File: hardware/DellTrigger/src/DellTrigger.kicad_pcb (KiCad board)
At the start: 2 copper layers, 30 x 12 mm, 11 parts, among them U1 U Eeprom DS2502 (TO92H)

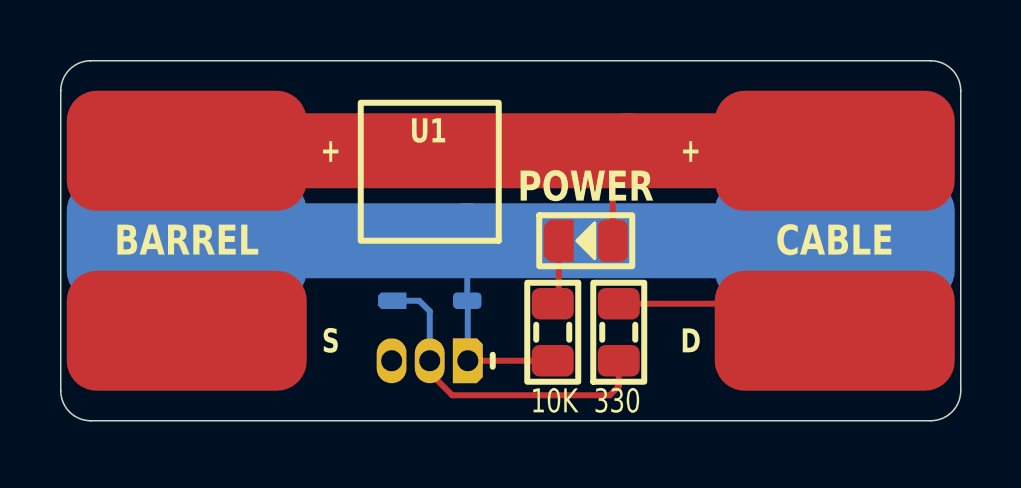
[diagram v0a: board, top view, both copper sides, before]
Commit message: Added DellTrigger schematics
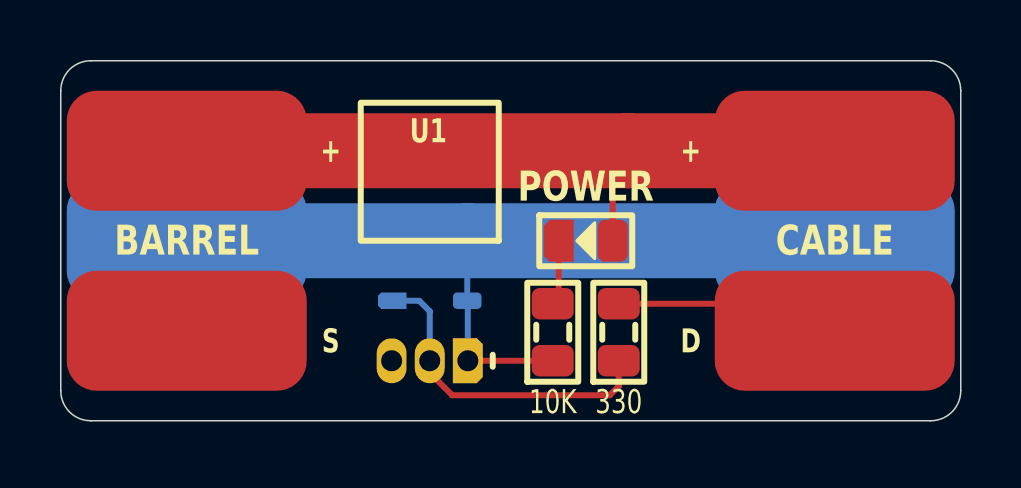
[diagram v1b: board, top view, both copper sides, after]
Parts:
- turned R2 to 90 degrees
- gave numbers to parts that had none: 6
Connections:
- net 20V renamed +VDC
- R2 pad 1: LED -> GND
- R2 pad 2: GND -> LED
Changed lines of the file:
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@@
 	(net 0 "")
 	(net 1 "GND")
-	(net 2 "20V")
+	(net 2 "DATA'")
 	(net 3 "DATA")
-	(net 4 "DATA'")
-	(net 5 "LED")
+	(net 4 "LED")
+	(net 5 "+VDC")
 	(footprint "Medo64:TP Pad (8.0x4.0)"
 		(locked yes)
@@
 		(at 40.8 18)
 		(descr "Keystone 5016")
-		(property "Reference" "TP?"
+		(property "Reference" "TP21"
 			(at 0 -3 0)
 			(layer "F.SilkS")
@@
 			(layers "F.Cu" "F.Mask")
 			(roundrect_rratio 0.25)
-			(net 2 "20V")
+			(net 5 "+VDC")
 		)
 	)
@@
 		(at 19.2 18)
 		(descr "Keystone 5016")
-		(property "Reference" "TP?"
+		(property "Reference" "TP11"
 			(at 0 -3 0)
 			(layer "F.SilkS")
@@
 			(layers "F.Cu" "F.Mask")
 			(roundrect_rratio 0.25)
-			(net 2 "20V")
+			(net 5 "+VDC")
 		)
 	)
@@
 			)
 		)
+		(property ki_fp_filters "LED* LED_SMD:* LED_THT:*")
+		(sheetname "Root")
+		(sheetfile "DellTrigger.kicad_sch")
 		(attr smd)
 		(fp_rect
@@
 			(chamfer_ratio 0.2)
 			(chamfer top_left bottom_left)
-			(net 5 "LED")
+			(net 4 "LED")
+			(pinfunction "K")
+			(pintype "passive")
 			(thermal_bridge_angle 45)
 		)
@@
 			(layers "F.Cu" "F.Paste" "F.Mask")
 			(roundrect_rratio 0.25)
-			(net 2 "20V")
+			(net 5 "+VDC")
+			(pinfunction "A")
+			(pintype "passive")
 			(thermal_bridge_angle 45)
 		)
@@
 		(at 19.2 24)
 		(descr "Keystone 5016")
-		(property "Reference" "TP?"
+		(property "Reference" "TP13"
 			(at 0 -3 0)
 			(layer "F.SilkS")
@@
 			)
 		)
+		(property ki_fp_filters "TO?92*")
+		(sheetname "Root")
+		(sheetfile "DellTrigger.kicad_sch")
 		(attr smd)
 		(fp_line
@@
 			(chamfer top_left bottom_left)
 			(net 1 "GND")
+			(pinfunction "GND")
+			(pintype "power_in")
 		)
 		(pad "2" thru_hole oval
@@
 			(remove_unused_layers no)
 			(net 3 "DATA")
+			(pinfunction "IO")
+			(pintype "bidirectional")
 		)
 		(pad "3" thru_hole oval
@@
 			(layers "*.Cu" "B.Mask")
 			(remove_unused_layers no)
+			(pinfunction "NC")
+			(pintype "no_connect")
 		)
 		(model "${KICAD8_3DMODEL_DIR}/Package_TO_SOT_THT.3dshapes/TO-92_Inline_W4.0mm_Horizontal_FlatSideDown.step"
@@
 		(at 40.8 24)
 		(descr "Keystone 5016")
-		(property "Reference" "TP?"
+		(property "Reference" "TP23"
 			(at 0 -3 0)
 			(layer "F.SilkS")
@@
 			(layers "F.Cu" "F.Mask")
 			(roundrect_rratio 0.25)
-			(net 4 "DATA'")
+			(net 2 "DATA'")
 		)
 	)
 	(footprint "Medo64:R (0805)"
 		(layer "F.Cu")
-		(at 31.4 24.05 -90)
+		(at 31.4 24.05 90)
 		(tags "RESC2013X70N")
 		(property "Reference" "R2"
@@
 		)
 		(property "Value" "10K"
-			(at 2.3 -0.05 0)
+			(at -2.325 0 180)
 			(layer "F.SilkS")
 			(effects
@@
 			)
 		)
+		(property ki_fp_filters "R_*")
+		(sheetname "Root")
+		(sheetfile "DellTrigger.kicad_sch")
 		(attr smd)
+		(fp_line
+			(start -0.25 -0.55)
+			(end 0.25 -0.55)
+			(stroke
+				(width 0.2)
+				(type default)
+			)
+			(layer "F.SilkS")
+		)
 		(fp_line
 			(start -0.25 0.55)
@@
 			(layer "F.SilkS")
 		)
-		(fp_line
-			(start -0.25 -0.55)
-			(end 0.25 -0.55)
+		(fp_rect
+			(start -1.65 -0.85)
+			(end 1.65 0.85)
 			(stroke
 				(width 0.2)
 				(type default)
 			)
-			(layer "F.SilkS")
-		)
-		(fp_rect
-			(start -1.65 -0.85)
-			(end 1.65 0.85)
-			(stroke
-				(width 0.2)
-				(type default)
-			)
 			(fill none)
 			(layer "F.SilkS")
@@
 		)
 		(pad "1" smd roundrect
-			(at -0.95 0 270)
-			(size 1.05 1.4)
-			(layers "F.Cu" "F.Paste" "F.Mask")
-			(roundrect_rratio 0.25)
-			(net 5 "LED")
-			(thermal_bridge_angle 45)
-		)
-		(pad "2" smd roundrect
-			(at 0.95 0 270)
+			(at -0.95 0 90)
 			(size 1.05 1.4)
 			(layers "F.Cu" "F.Paste" "F.Mask")
 			(roundrect_rratio 0.25)
 			(net 1 "GND")
+			(pintype "passive")
+			(thermal_bridge_angle 45)
+		)
+		(pad "2" smd roundrect
+			(at 0.95 0 90)
+			(size 1.05 1.4)
+			(layers "F.Cu" "F.Paste" "F.Mask")
+			(roundrect_rratio 0.25)
+			(net 4 "LED")
+			(pintype "passive")
 			(thermal_bridge_angle 45)
 		)
@@
 		)
 		(property "Value" "330"
-			(at -2.3 -0.05 360)
+			(at -2.325 0 0)
 			(layer "F.SilkS")
 			(effects
@@
 			)
 		)
+		(property ki_fp_filters "R_*")
+		(sheetname "Root")
+		(sheetfile "DellTrigger.kicad_sch")
 		(attr smd)
 		(fp_line
@@
 			(roundrect_rratio 0.25)
 			(net 3 "DATA")
+			(pintype "passive")
 			(thermal_bridge_angle 45)
 		)
@@
 			(layers "F.Cu" "F.Paste" "F.Mask")
 			(roundrect_rratio 0.25)
-			(net 4 "DATA'")
+			(net 2 "DATA'")
+			(pintype "passive")
 			(thermal_bridge_angle 45)
 		)
@@
 		)
 		(property "Value" "CUS08F30"
-			(at 0 -1.6 360)
+			(at 0 -1.6 0)
 			(layer "B.Fab")
 			(hide yes)
@@
 		)
 		(property "Footprint" "Medo64:D (SOD323)"
-			(at 0 0 360)
+			(at 0 0 0)
 			(layer "B.Fab")
 			(hide yes)
@@
 		)
 		(property "Datasheet" ""
-			(at 0 0 360)
+			(at 0 0 0)
 			(layer "B.Fab")
 			(hide yes)
@@
 		)
 		(property "Description" ""
-			(at 0 0 360)
+			(at 0 0 0)
 			(layer "B.Fab")
 			(hide yes)
@@
 			)
 		)
+		(property ki_fp_filters "TO-???* *_Diode_* *SingleDiode* D_*")
+		(sheetname "Root")
+		(sheetfile "DellTrigger.kicad_sch")
 		(attr smd)
 		(fp_line
@@
 		)
 		(fp_text user "C"
-			(at -1.25 0.4 360)
+			(at -1.25 0.4 0)
 			(layer "Cmts.User" knockout)
 			(effects
@@
 		)
 		(fp_text user "A"
-			(at 1.25 0.4 360)
+			(at 1.25 0.4 0)
 			(layer "Cmts.User" knockout)
 			(effects
@@
 			(chamfer top_left bottom_left)
 			(net 3 "DATA")
+			(pinfunction "K")
+			(pintype "passive")
 			(thermal_bridge_angle 45)
 		)
@@
 			(roundrect_rratio 0.25)
 			(net 1 "GND")
+			(pinfunction "A")
+			(pintype "passive")
 			(thermal_bridge_angle 45)
 		)
@@
 		(at 19.2 21 180)
 		(descr "Keystone 5016")
-		(property "Reference" "TP?"
+		(property "Reference" "TP12"
 			(at 0 3 0)
 			(layer "B.SilkS")
@@
 		(at 40.8 21 180)
 		(descr "Keystone 5016")
-		(property "Reference" "TP?"
+		(property "Reference" "TP22"
 			(at 0 3 0)
 			(layer "B.SilkS")
@@
 	)
 	(segment
-		(start 33.9 18)
-		(end 19.2 18)
-		(width 2.5)
-		(layer "F.Cu")
-		(net 2)
-	)
-	(segment
-		(start 40.8 18)
-		(end 33.9 18)
-		(width 2.5)
-		(layer "F.Cu")
-		(net 2)
-	)
-	(segment
-		(start 33.4 21)
-		(end 33.4 18.5)
-		(width 0.2)
-		(layer "F.Cu")
-		(net 2)
-	)
-	(segment
-		(start 33.4 18.5)
-		(end 33.9 18)
+		(start 33.6 23.1)
+		(end 39.9 23.1)
 		(width 0.2)
 		(layer "F.Cu")
@@
 	)
 	(segment
-		(start 33.6 23.1)
-		(end 39.9 23.1)
-		(width 0.2)
-		(layer "F.Cu")
-		(net 4)
-	)
-	(segment
 		(start 31.6 21)
 		(end 31.6 22.9)
 		(width 0.2)
 		(layer "F.Cu")
+		(net 4)
+	)
+	(segment
+		(start 33.9 18)
+		(end 19.2 18)
+		(width 2.5)
+		(layer "F.Cu")
+		(net 5)
+	)
+	(segment
+		(start 40.8 18)
+		(end 33.9 18)
+		(width 2.5)
+		(layer "F.Cu")
+		(net 5)
+	)
+	(segment
+		(start 33.4 21)
+		(end 33.4 18.5)
+		(width 0.2)
+		(layer "F.Cu")
+		(net 5)
+	)
+	(segment
+		(start 33.4 18.5)
+		(end 33.9 18)
+		(width 0.2)
+		(layer "F.Cu")

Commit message: Changed DellTrigger diode to zener
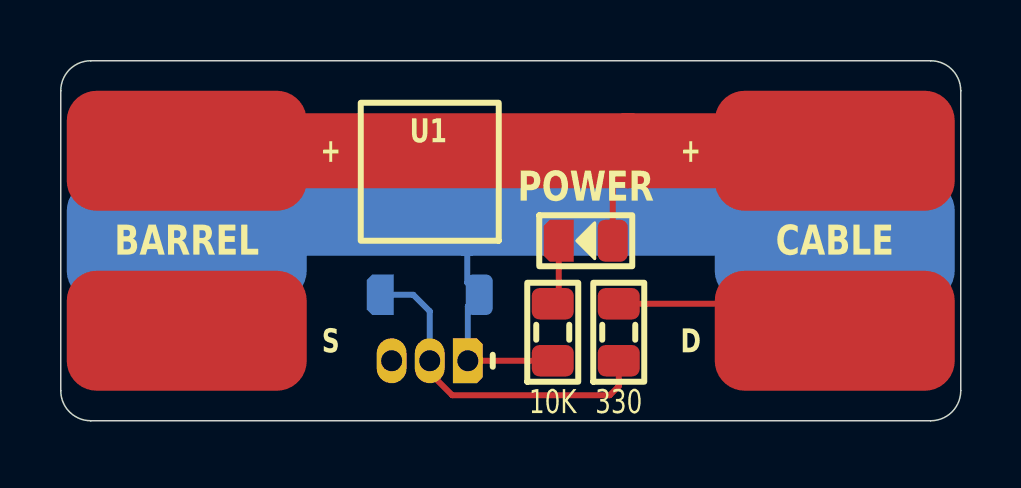
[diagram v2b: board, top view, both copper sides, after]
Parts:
- D1: footprint Medo64:D (SOD323) -> Medo64:D Zener (SOD80C)
- moved D1 0.20 mm to (27.3, 22.8)
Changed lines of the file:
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@@
 		)
 	)
-	(footprint "Medo64:D (SOD323)"
-		(layer "B.Cu")
-		(at 27.3 23)
-		(descr "CUS08F30,H3F")
-		(tags "SOD2612X116N")
+	(footprint "Medo64:D Zener (SOD80C)"
+		(layer "B.Cu")
+		(at 27.3 22.8)
+		(descr "Nexperia BZV55-B5V1,115")
 		(property "Reference" "D1"
-			(at 0 -1.55 0)
+			(at 0.175 0.025 180)
 			(layer "B.SilkS")
 			(effects
@@
 		)
 		(property "Value" "CUS08F30"
-			(at 0 -1.6 0)
+			(at 0 -1.9 180)
 			(layer "B.Fab")
 			(hide yes)
@@
 			)
 		)
-		(property "Footprint" "Medo64:D (SOD323)"
-			(at 0 0 0)
+		(property "Footprint" "Medo64:D Zener (SOD80C)"
+			(at 0 0 180)
 			(layer "B.Fab")
 			(hide yes)
@@
 		)
 		(property "Datasheet" ""
-			(at 0 0 0)
+			(at 0 0 180)
 			(layer "B.Fab")
 			(hide yes)
@@
 		)
 		(property "Description" ""
-			(at 0 0 0)
+			(at 0 0 180)
 			(layer "B.Fab")
 			(hide yes)
@@
 		(attr smd)
 		(fp_line
-			(start -0.55 -0.52)
-			(end -0.55 0.52)
+			(start -0.6 -0.725)
+			(end -0.6 0.725)
 			(stroke
 				(width 0.2)
@@
 		)
 		(fp_line
-			(start 0.55 -0.52)
-			(end -0.55 -0.52)
+			(start -0.1 0.725)
+			(end -0.6 0.725)
 			(stroke
 				(width 0.2)
@@
 		)
 		(fp_line
-			(start 0.55 0.52)
-			(end -0.55 0.52)
+			(start 0.6 -0.725)
+			(end -0.6 -0.725)
 			(stroke
 				(width 0.2)
@@
 		)
 		(fp_rect
-			(start 1.9 -0.85)
-			(end -1.9 0.85)
+			(start 2.2 -1.05)
+			(end -2.2 1.05)
 			(stroke
 				(width 0.2)
@@
 		)
 		(fp_circle
-			(center -2.3 0)
-			(end -2.15 0)
+			(center -2.6 0)
+			(end -2.45 0)
 			(stroke
 				(width 0.1)
@@
 		)
 		(fp_rect
-			(start 2 -0.95)
-			(end -2 0.95)
+			(start 2.3 -1.15)
+			(end -2.3 1.15)
 			(stroke
 				(width 0.01)
@@
 		)
 		(fp_rect
-			(start 0.825 -0.62)
-			(end -0.825 0.62)
+			(start 1.65 -0.8)
+			(end -1.65 0.8)
 			(stroke
 				(width 0.01)
@@
 			(layer "B.Fab")
 		)
-		(fp_text user "C"
-			(at -1.25 0.4 0)
+		(fp_text user "A"
+			(at 1.475 0.75 180)
 			(layer "Cmts.User" knockout)
 			(effects
@@
 			)
 		)
-		(fp_text user "A"
-			(at 1.25 0.4 0)
+		(fp_text user "C"
+			(at -1.475 0.75 180)
 			(layer "Cmts.User" knockout)
 			(effects
@@
 		)
 		(pad "1" smd roundrect
-			(at -1.25 0)
-			(size 0.95 0.55)
+			(at -1.65 0)
+			(size 0.9 1.35)
 			(layers "B.Cu" "B.Paste" "B.Mask")
 			(roundrect_rratio 0.25)
@@
 		)
 		(pad "2" smd roundrect
-			(at 1.25 0)
-			(size 0.95 0.55)
+			(at 1.65 0)
+			(size 0.9 1.35)
 			(layers "B.Cu" "B.Paste" "B.Mask")
 			(roundrect_rratio 0.25)
@@
 			(thermal_bridge_angle 45)
 		)
-		(model "${KICAD8_3DMODEL_DIR}/Diode_SMD.3dshapes/D_SOD-323.wrl"
+		(model "${KICAD8_3DMODEL_DIR}/Diode_SMD.3dshapes/D_MiniMELF.step"
 			(offset
 				(xyz 0 0 0)
@@
 	)
 	(segment
+		(start 28.55 22.4)
+		(end 28.55 21)
+		(width 0.2)
+		(layer "B.Cu")
+		(net 1)
+	)
+	(segment
+		(start 28.95 22.8)
+		(end 28.55 22.4)
+		(width 0.2)
+		(layer "B.Cu")
+		(net 1)
+	)
+	(segment
+		(start 28.57 23.18)
+		(end 28.95 22.8)
+		(width 0.2)
+		(layer "B.Cu")
+		(net 1)
+	)
+	(segment
+		(start 19.175 20.25)
+		(end 28.525 20.25)
+		(width 2.5)
+		(layer "B.Cu")
+		(net 1)
+	)
+	(segment
+		(start 28.55 20.25)
+		(end 40.8 20.25)
+		(width 2.5)
+		(layer "B.Cu")
+		(net 1)
+	)
+	(segment
 		(start 28.57 25)
-		(end 28.57 23.02)
-		(width 0.2)
-		(layer "B.Cu")
-		(net 1)
-	)
-	(segment
-		(start 19.2 21)
-		(end 28.55 21)
-		(width 2.5)
-		(layer "B.Cu")
-		(net 1)
-	)
-	(segment
-		(start 28.55 21)
-		(end 40.8 21)
-		(width 2.5)
-		(layer "B.Cu")
-		(net 1)
-	)
-	(segment
-		(start 28.55 23)
-		(end 28.55 21)
+		(end 28.57 23.18)
 		(width 0.2)
 		(layer "B.Cu")
@@
 	)
 	(segment
-		(start 27.3 23.35)
-		(end 26.95 23)
-		(width 0.2)
-		(layer "B.Cu")
-		(net 3)
-	)
-	(segment
-		(start 26.95 23)
-		(end 26.05 23)
-		(width 0.2)
-		(layer "B.Cu")
-		(net 3)
-	)
-	(segment
 		(start 27.3 25)
 		(end 27.3 23.35)
 		(width 0.2)
 		(layer "B.Cu")
+		(net 3)
+	)
+	(segment
+		(start 27.3 23.35)
+		(end 26.75 22.8)
+		(width 0.2)
+		(layer "B.Cu")
+		(net 3)
+	)
+	(segment
+		(start 26.75 22.8)
+		(end 25.65 22.8)
+		(width 0.2)
+		(layer "B.Cu")
